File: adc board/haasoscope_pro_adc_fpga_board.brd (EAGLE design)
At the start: 224.5 x 160 mm, 639 parts, among them CN2 12Vin, IC1 ADC12DL2500ACF, IC10 TPS72325DBVR, IC13 LMH5401IRMST, IC14 LMH6401IRMZR, IC15 SN74AVC4T774PWR, IC17 DAC8562SDGSR, IC18 TLV9102IPWR, IC2 SN74AVC4T774PWR, IC21 LMH5401IRMST, IC22 TPS7A7200RGTR, IC23 TPS7A7200RGTR, IC24 TPS7A7200RGTR, IC25 TPS72325DBVR, IC26 TPS7A7200RGTR, IC27 TPS7A7200RGTR, IC28 TPS7A7200RGTR, IC29 LMH6401IRMZR, IC3 ADC122S021CIMM_NOPB, IC30 SN74AVC4T774PWR, IC33 TLV9102IPWR, IC4 TLV9102IPWR, IC5 EP4CE30F23C6N, IC6 EPCQ16ASI8N, IC7 TPS7A7200RGTR, IC8 FT232HQ, IC9 93LC56B, J11 8pin, J15 test1, J2 test1, J3 2p-2.54, J30 2p-2.54, J31 2p-2.54, J32 2p-2.54, J33 2p-2.54, J34 2p-2.54, J35 2p-2.54, J36 2p-2.54, J37 2p-2.54, J39 2p-2.54, J4 2p-2.54, J40 2p-2.54, J41 2p-2.54, J42 2p-2.54, J43 2p-2.54, J44 2p-2.54, J45 2p-2.54, J46 2p-2.54, K1 G6K-2F-RF-T-TR03_DC5, K2 G6K-2F-RF-T-TR03_DC5, K3 G6K-2F-RF-T-TR03_DC5, K4 G6K-2F-RF-T-TR03_DC5, K5 G6K-2F-RF-T-TR03_DC5, K6 TLP3475_TP,F, K7 TLP3475_TP,F, Q1 S8050, Q2 FDN340P, Q4 S8050, Q5 S8050, Q7 S8050, Q8 S8050, Q9 S8050, SW3 SKQGADE010, SW4 SKQGADE010, U1 WS2812-2020, U2 ADF4350BCPZ, U3 WS2812-2020, U4 725996-2, U5 725996-2, X1 USBC, Y2 OSCILLATORSMD-5X3, Y3 12MHz

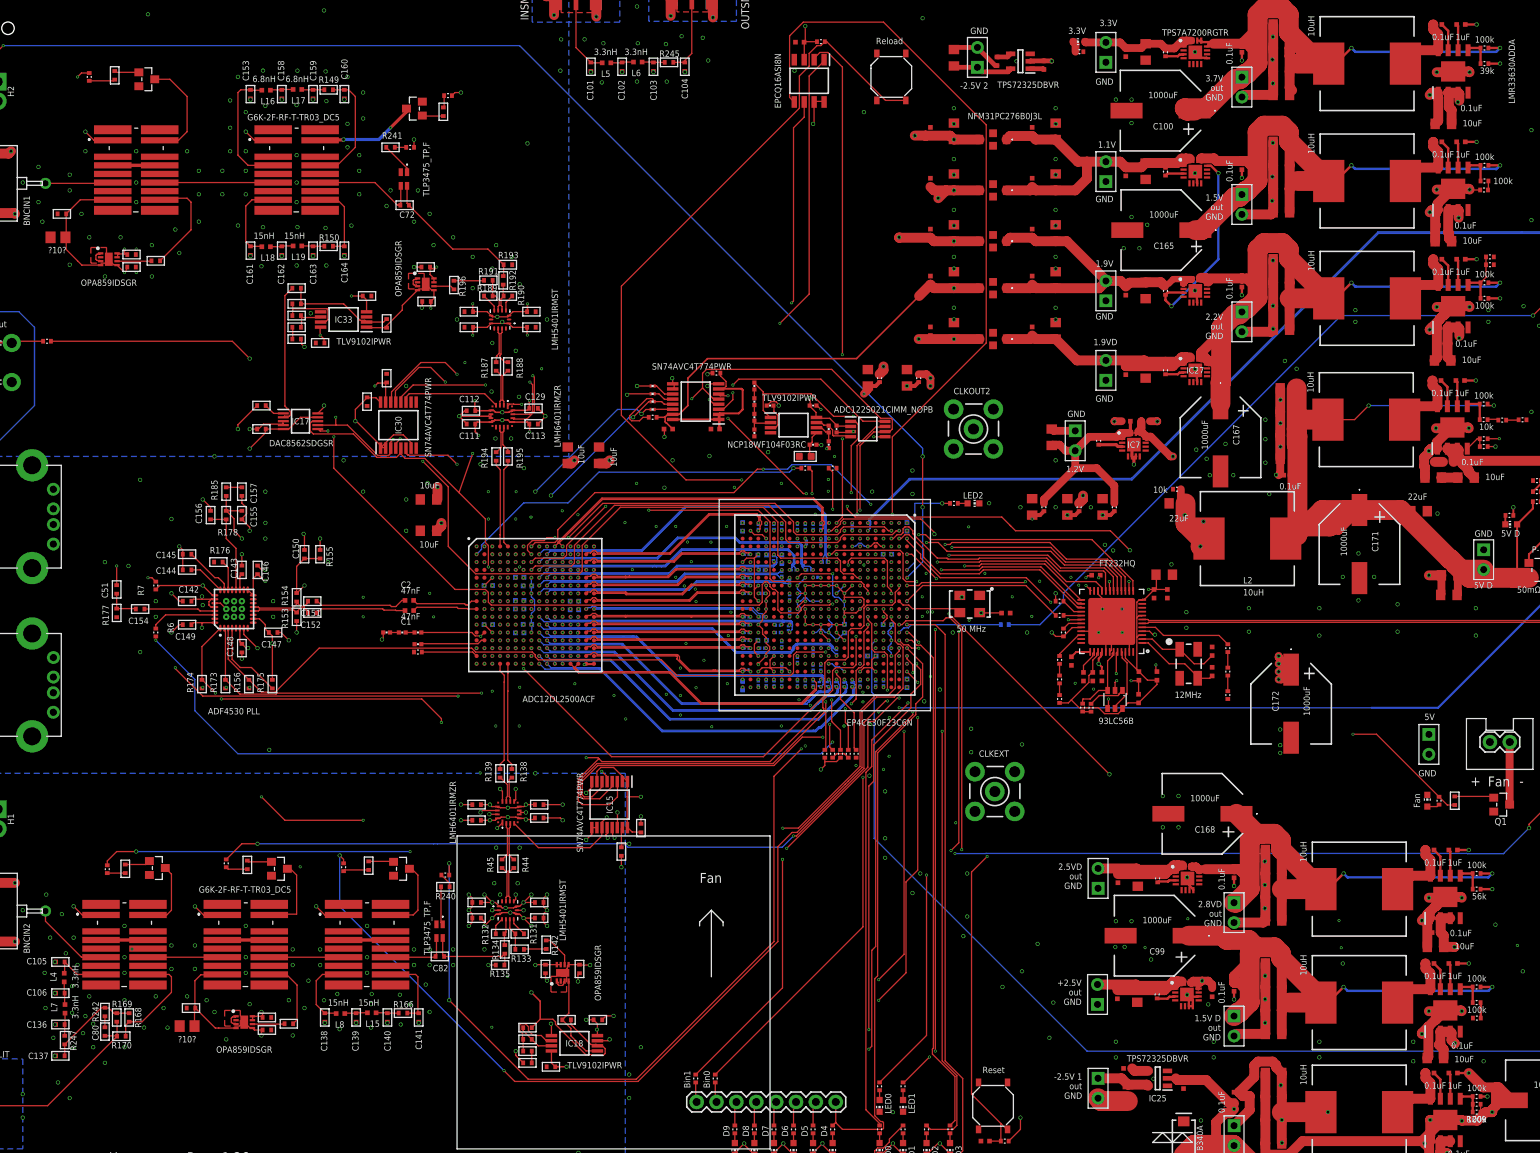
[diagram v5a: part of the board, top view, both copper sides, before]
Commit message: move pads a little (~2 mil) closer for MF_PASSIVES R and C 0402 package, to fix JLCPCB complaint
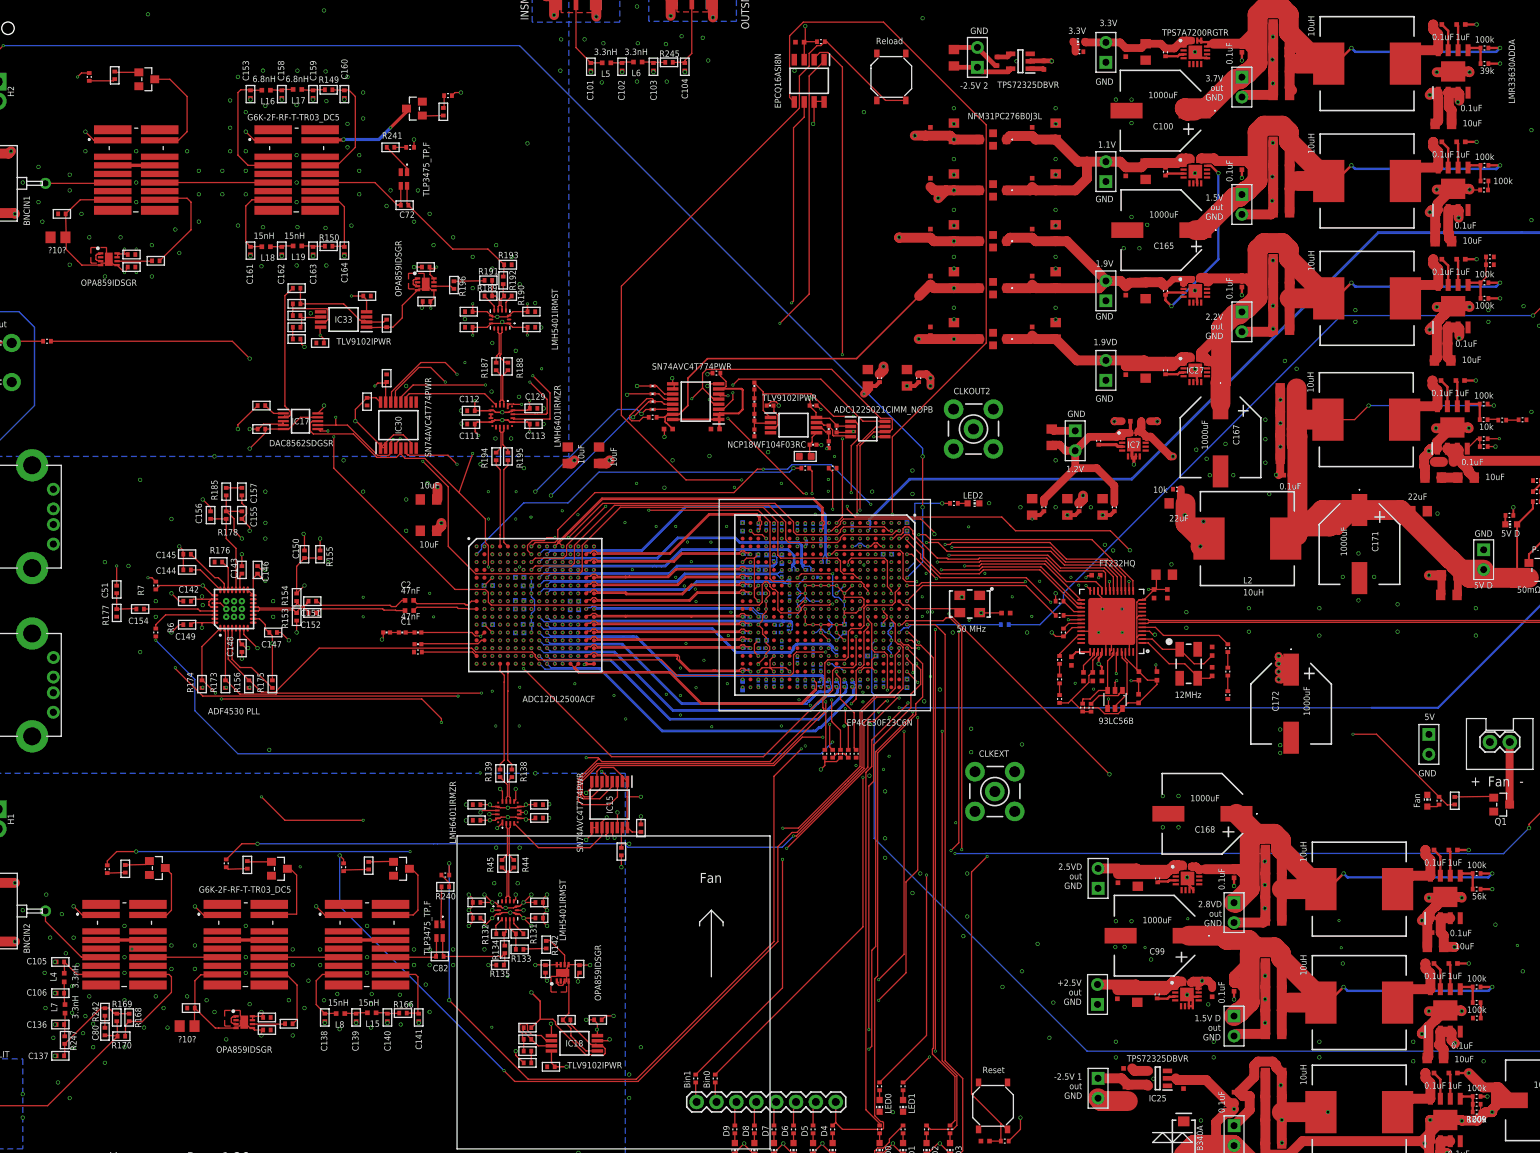
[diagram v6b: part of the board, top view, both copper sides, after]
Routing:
- net GND: track 519.4 -> 502.8 mm, vias 760 -> 763
- net AMPSCLK2: track 29.5 -> 32.9 mm
- net AMPSCS2: track 27.2 -> 30.0 mm
- net 2V5+: track 152.9 -> 153.7 mm

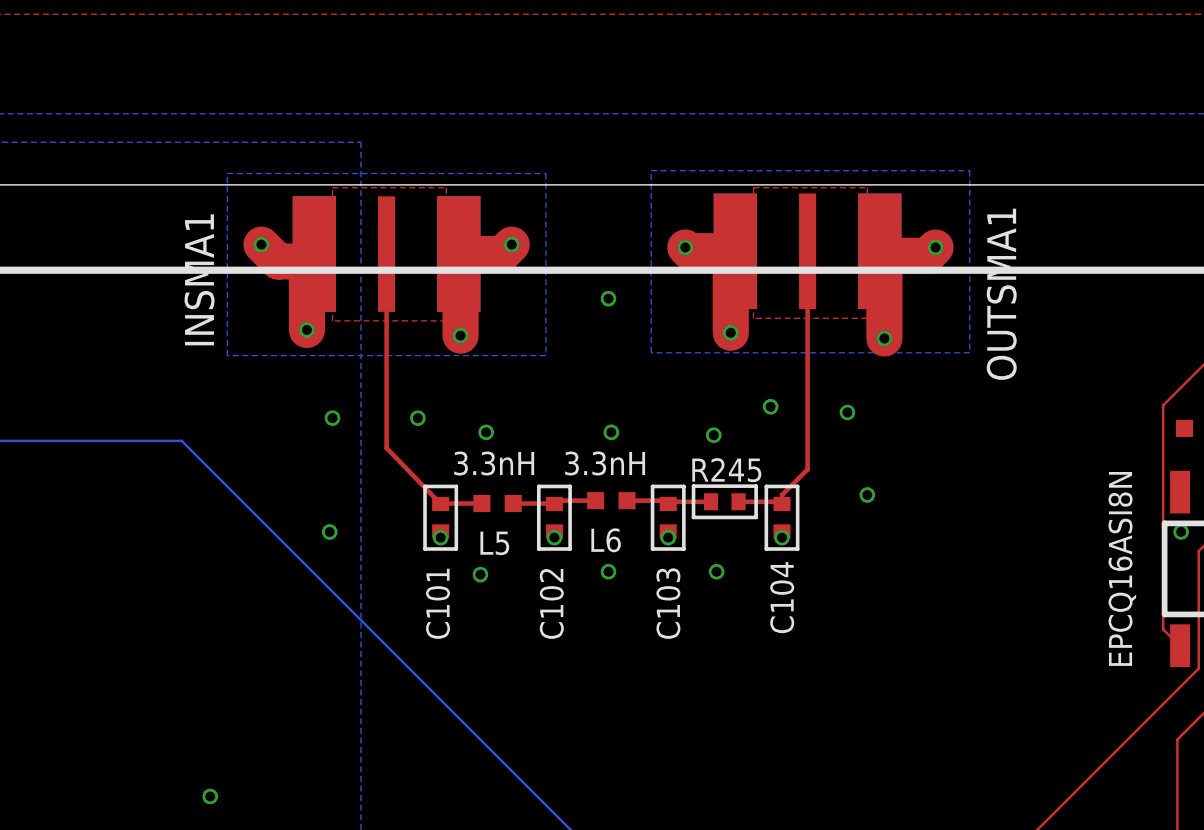
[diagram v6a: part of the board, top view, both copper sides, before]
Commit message: remove test filter
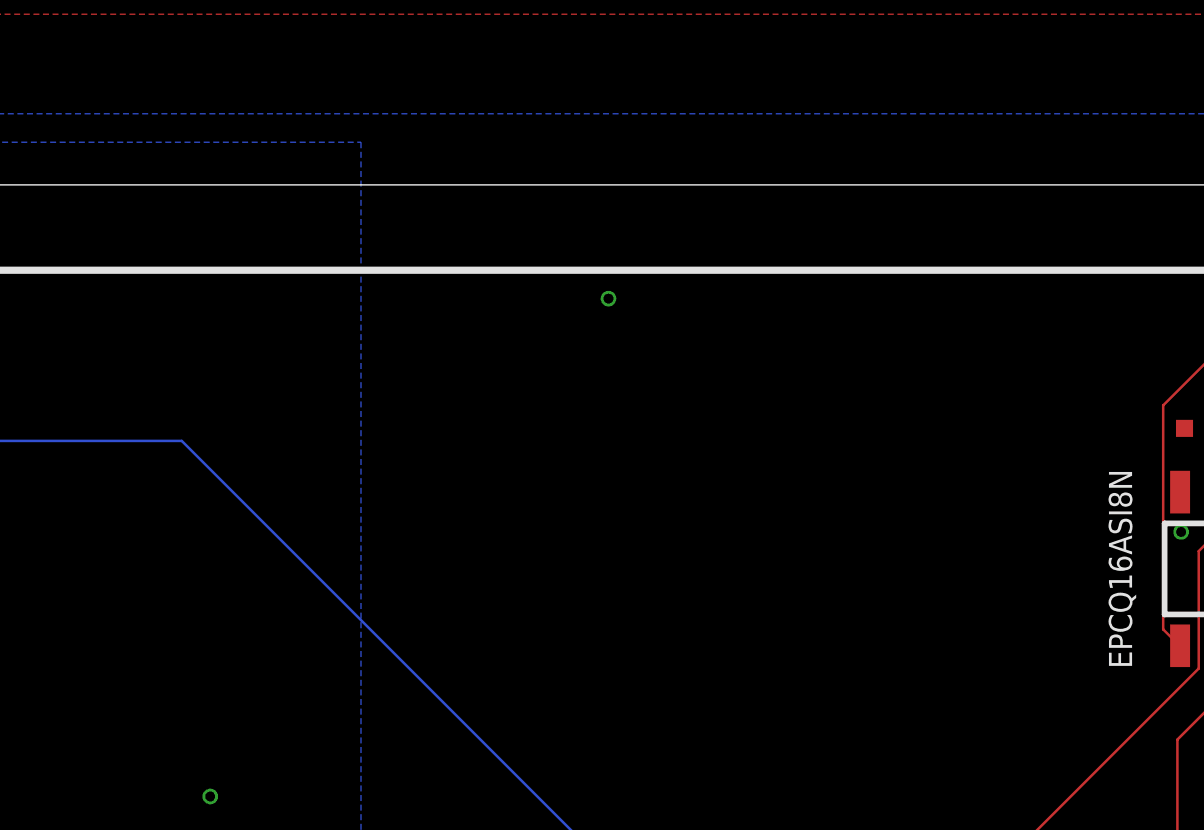
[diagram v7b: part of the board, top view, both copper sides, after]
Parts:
- removed C101: 1.0pF, MF_Passives:C0402
- removed C102: 0.75pF, MF_Passives:C0402
- removed C103: 0.5pF, MF_Passives:C0402
- removed C104: ?0?, MF_Passives:C0402
- removed INSMA1, OUTSMA1: 50, adafruit:SMA_EDGELAUNCH
- removed L5, L6: 3.3nH, Nordic_nRF:RESC0402_N
- removed R245: 0, MF_Passives:R0402
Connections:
- removed net N$71: C102.P$1, L5.2, L6.1
- removed net N$72: C103.P$1, L6.2, R245.P$2
- removed net SMAIN2: C101.P$1, INSMA1.P, L5.1
- removed net SMAOUT2: C104.P$1, OUTSMA1.P, R245.P$1
- net GND: no longer C101.P$2, C102.P$2, C103.P$2, C104.P$2, INSMA1.GND@1, INSMA1.GND@2, INSMA1.GND@3, INSMA1.GND@4, OUTSMA1.GND@1, OUTSMA1.GND@2, OUTSMA1.GND@3, OUTSMA1.GND@4
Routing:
- net GND: track 502.8 -> 483.5 mm, vias 763 -> 739
- net SMAIN2: track 11.0 -> 0.00 mm
- net SMAOUT2: track 10.9 -> 0.00 mm
- net N$72: track 3.10 -> 0.00 mm
- net N$71: track 2.98 -> 0.00 mm

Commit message: 1k for 12VConnected
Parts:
- R237: value 10k -> 1k
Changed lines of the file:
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@@
 <attribute name="MPN" value="P-MOS AO3401A" x="210.64" y="87.01" size="0.8128" layer="21" rot="R180"/>
 </element>
-<element name="R237" library="FlashPCB_Resistors" package="RES-0402" value="10k" x="202.99" y="92.72" smashed="yes" rot="R180"/>
+<element name="R237" library="FlashPCB_Resistors" package="RES-0402" value="1k" x="202.99" y="92.72" smashed="yes" rot="R180"/>
 <element name="R238" library="FlashPCB_Resistors" package="RES-0402" value="1k" x="205.1" y="95.41" smashed="yes"/>
 <element name="R239" library="FlashPCB_Resistors" package="RES-0402" value="10k" x="205.09" y="94.01" smashed="yes"/>
@@
 <via x="100" y="78.6" extent="1-16" drill="0.2"/>
 <via x="94.05" y="81.95" extent="1-16" drill="0.2"/>
-<wire x1="66.23" y1="102.69" x2="66.2974" y2="102.64" width="0.2" layer="1"/>
 <wire x1="69.33" y1="103.39" x2="69.33" y2="103.89" width="0.2" layer="1"/>
 <wire x1="59.5" y1="122.7" x2="60.5174" y2="122.7" width="0.2" layer="1"/>
